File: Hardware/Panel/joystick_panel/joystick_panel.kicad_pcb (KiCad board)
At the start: 2 copper layers, 100 x 200 mm, 17 parts

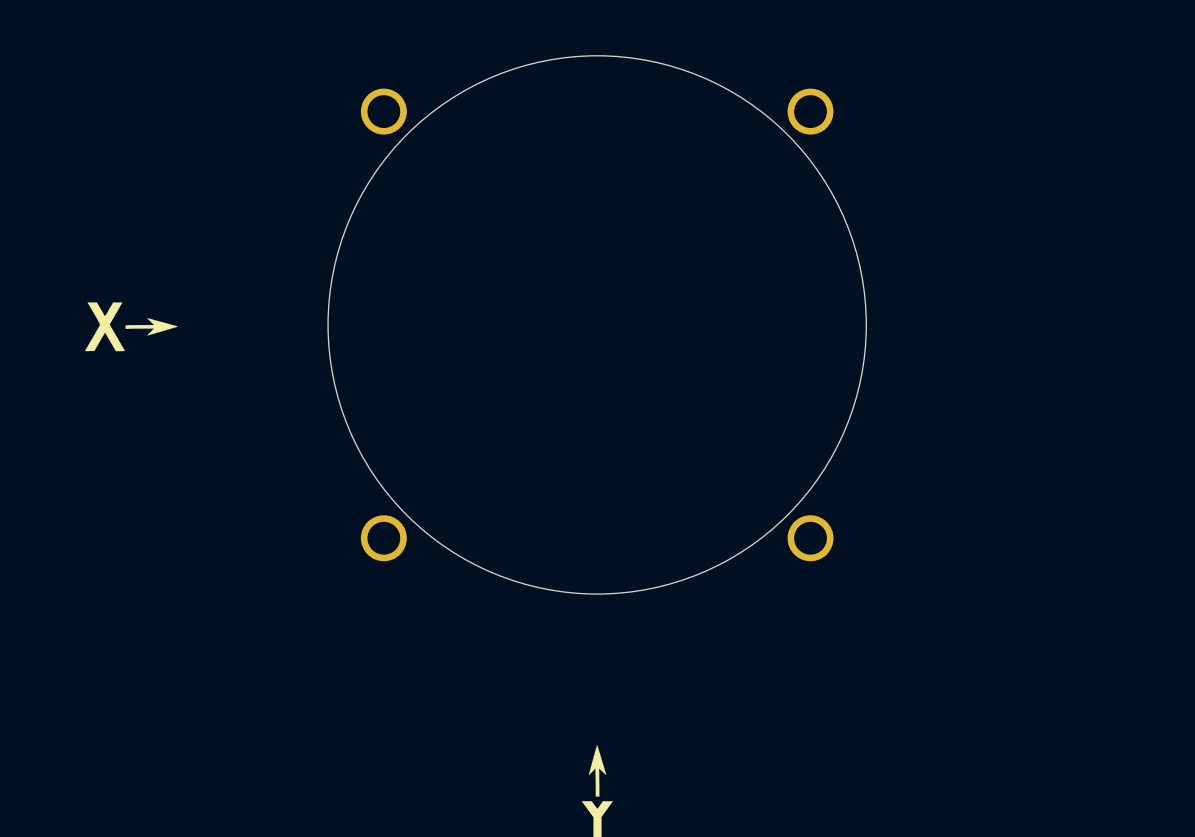
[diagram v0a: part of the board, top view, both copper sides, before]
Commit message: Belated .gitignore; switch to panel mounted pots implying board and panel changes
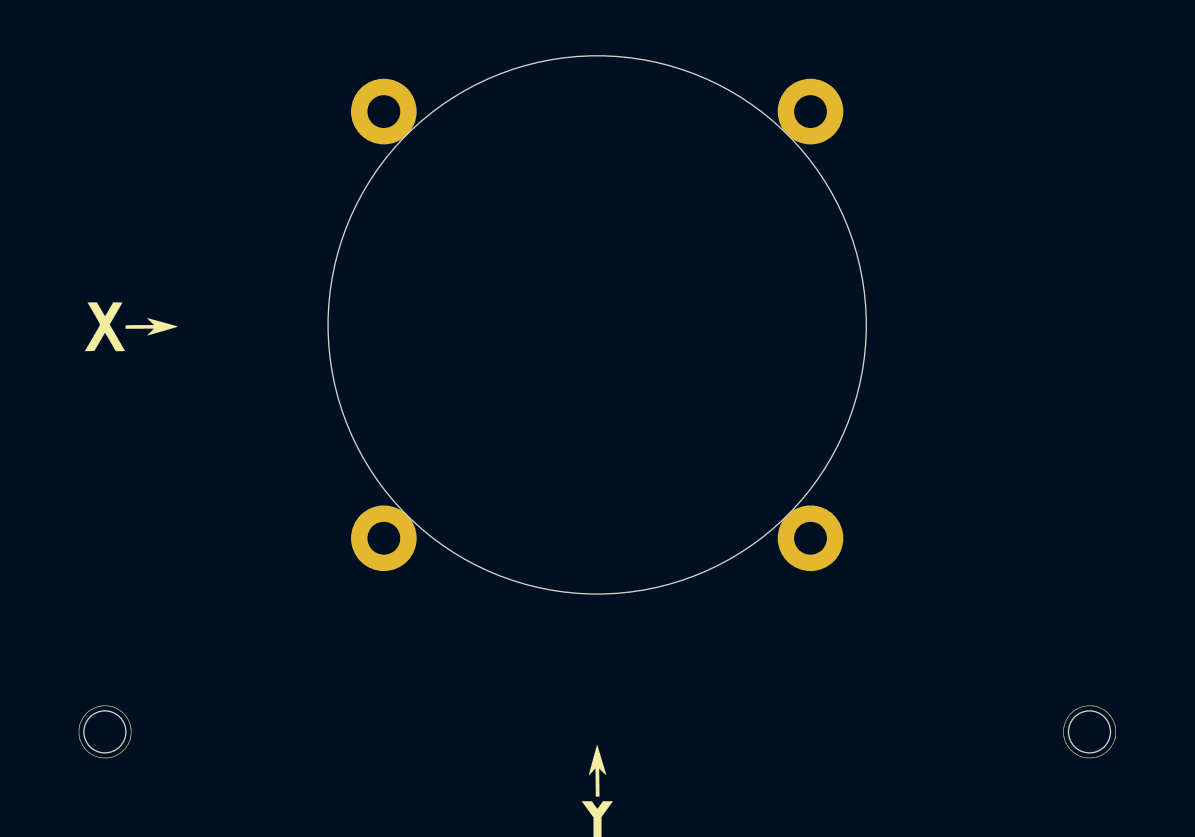
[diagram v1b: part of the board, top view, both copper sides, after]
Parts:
- added H15: Mounting_Hole, ao_tht:MountingHole_3.2mm_M3, F.Cu at (28.6, 88.6)
- added H16: Mounting_Hole, ao_tht:MountingHole_3.2mm_M3, F.Cu at (103.6, 88.6)

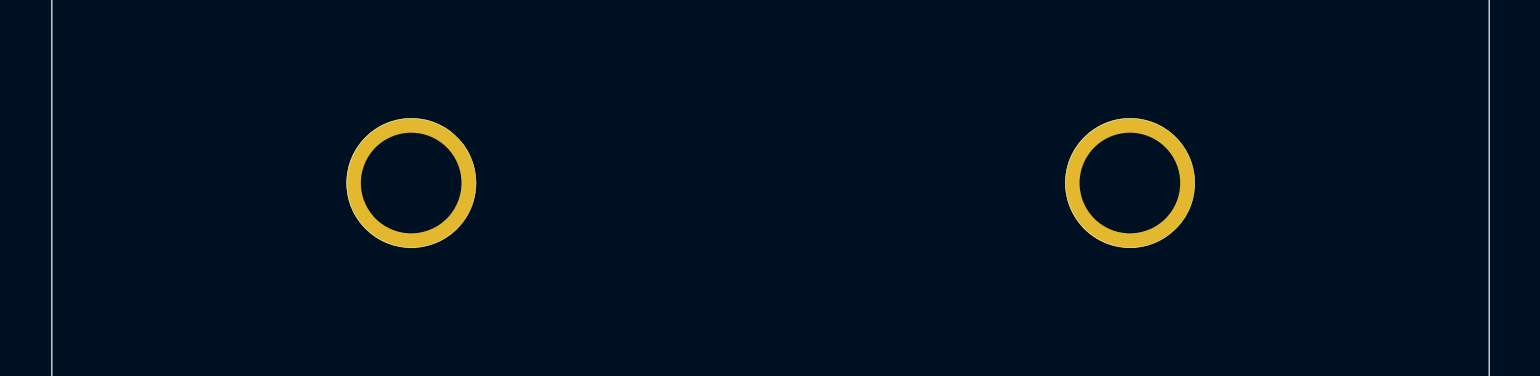
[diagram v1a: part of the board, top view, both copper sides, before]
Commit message: Add gain trimmers and test points
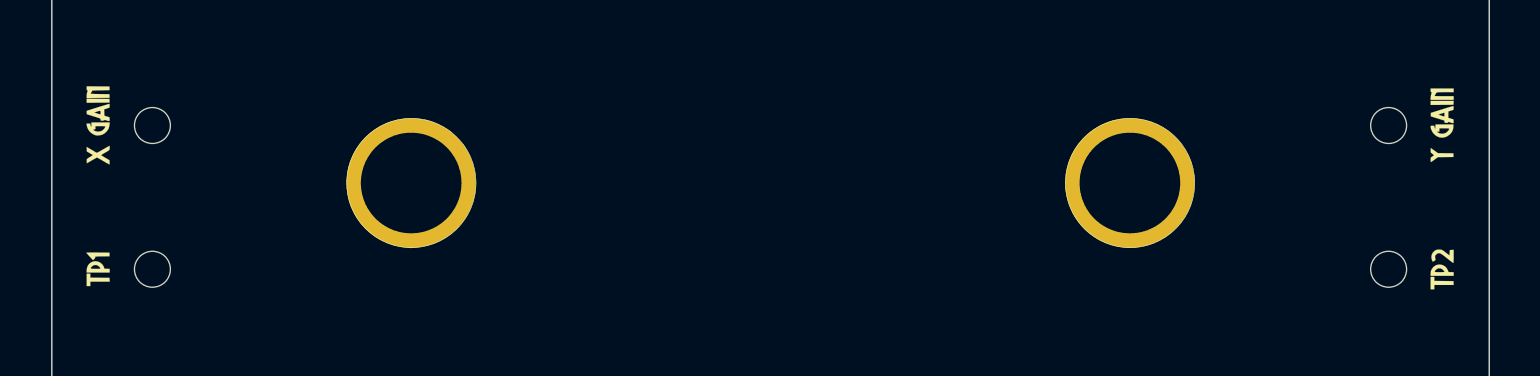
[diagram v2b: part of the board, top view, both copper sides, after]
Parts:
- added H17: Trimmer_Hole, Kosmo_panel:Kosmo_Trimmer_Pot_Hole, F.Cu at (23.1, 143.6)
- added H18: Trimmer_Hole, Kosmo_panel:Kosmo_Trimmer_Pot_Hole, F.Cu at (109.1, 143.6)
- added H19: Trimmer_Hole, Kosmo_panel:Kosmo_Trimmer_Pot_Hole, F.Cu at (23.1, 153.6)
- added H20: Trimmer_Hole, Kosmo_panel:Kosmo_Trimmer_Pot_Hole, F.Cu at (109.1, 153.6)

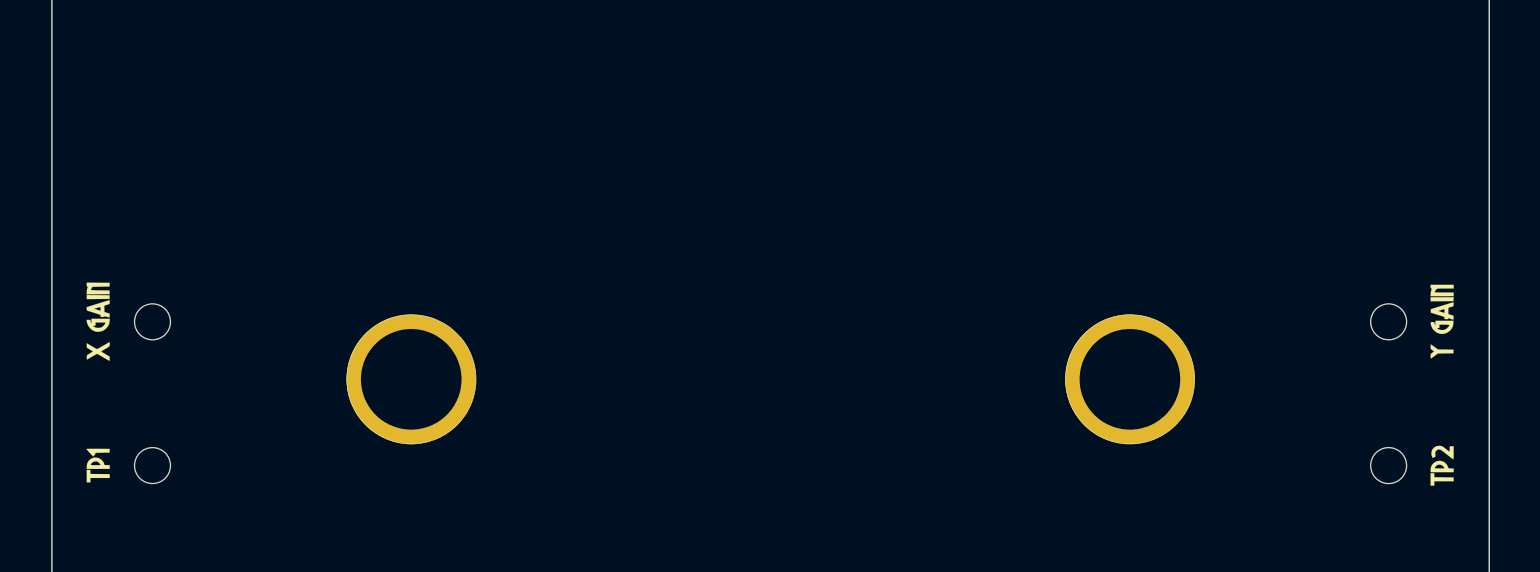
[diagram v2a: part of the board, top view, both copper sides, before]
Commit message: Move trimmers to inputs
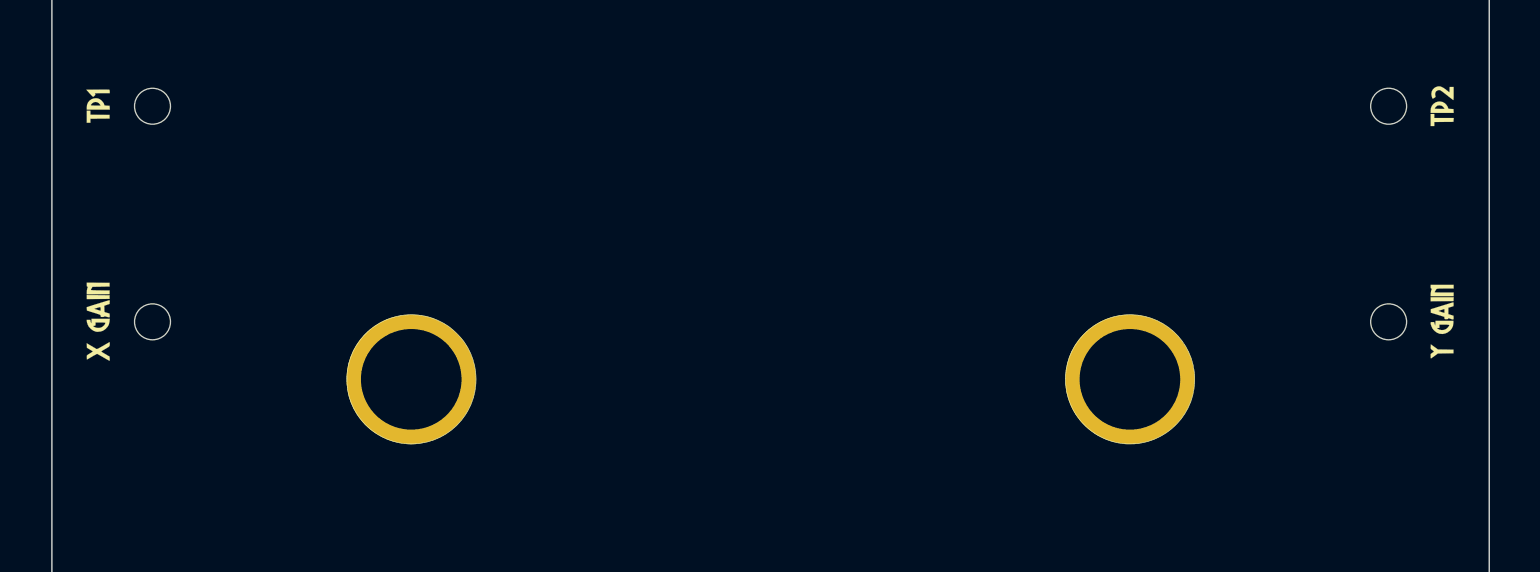
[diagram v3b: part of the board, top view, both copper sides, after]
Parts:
- moved H19 25.0 mm to (23.1, 128.6)
- moved H20 25.0 mm to (109.1, 128.6)

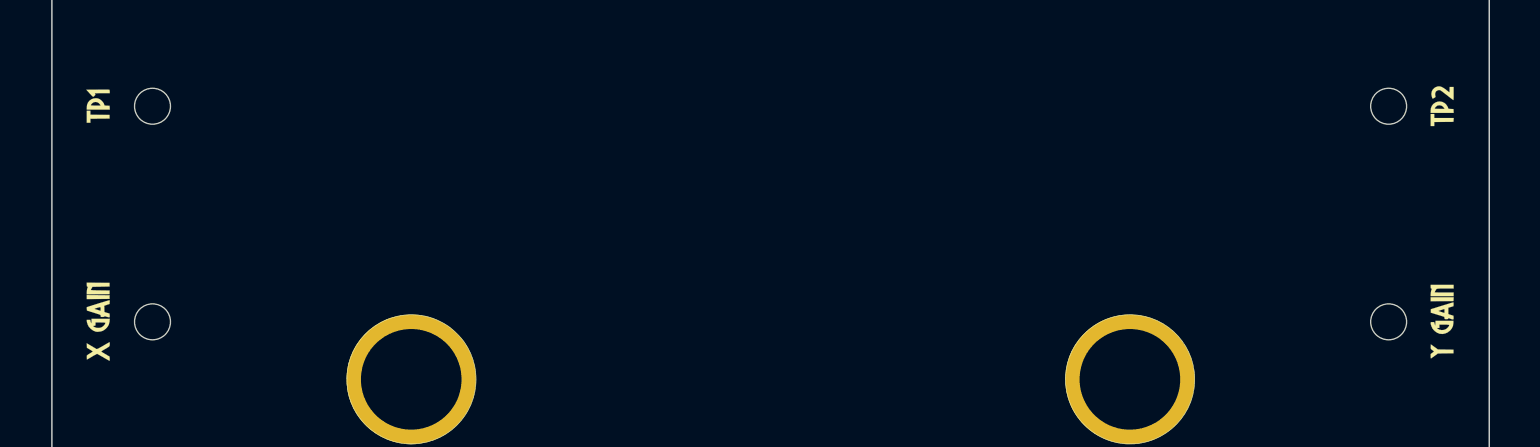
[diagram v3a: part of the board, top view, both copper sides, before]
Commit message: Move trimmers and TPs to back
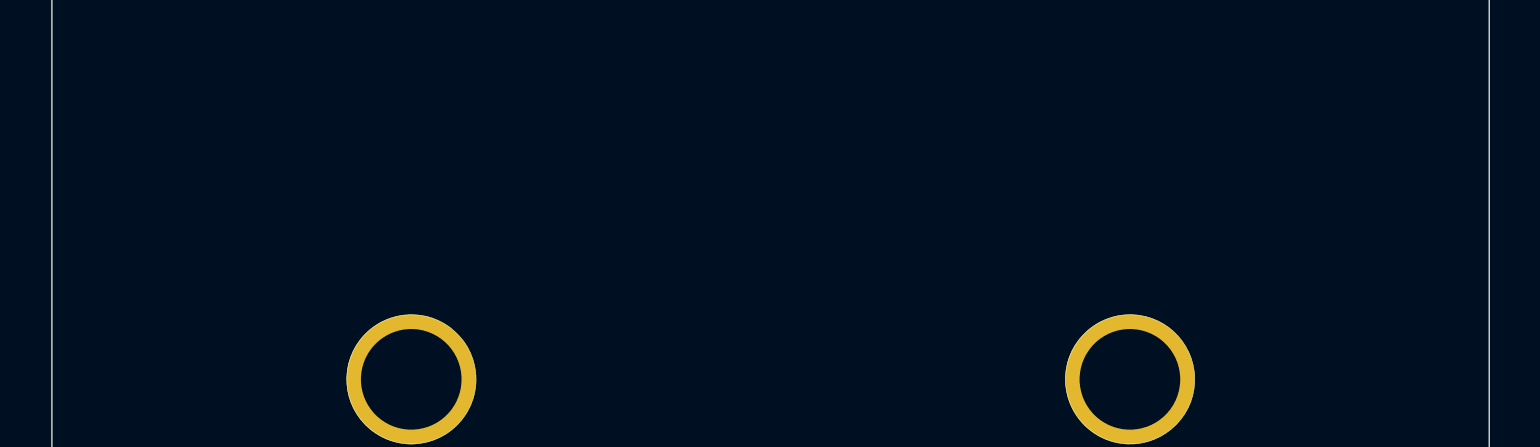
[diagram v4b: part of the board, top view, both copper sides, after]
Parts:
- removed H17, H18, H19, H20: Trimmer_Hole, Kosmo_panel:Kosmo_Trimmer_Pot_Hole

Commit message: Gerbers
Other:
- net class Default removed
